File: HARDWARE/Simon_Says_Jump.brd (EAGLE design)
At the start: 57.1 x 88.9 mm, 35 parts, among them J1 RJ45, J2 RJ45, J3 RJ45, J4 RJ45, J6 5V, Q1 NPN, Q2 P-Channel MOSFET, Q3 NPN, Q4 P-Channel MOSFET, Q5 NPN, Q6 P-Channel MOSFET, Q7 NPN, Q8 P-Channel MOSFET, U1 3.3V Pro Mini, U2 RFM69_BOB

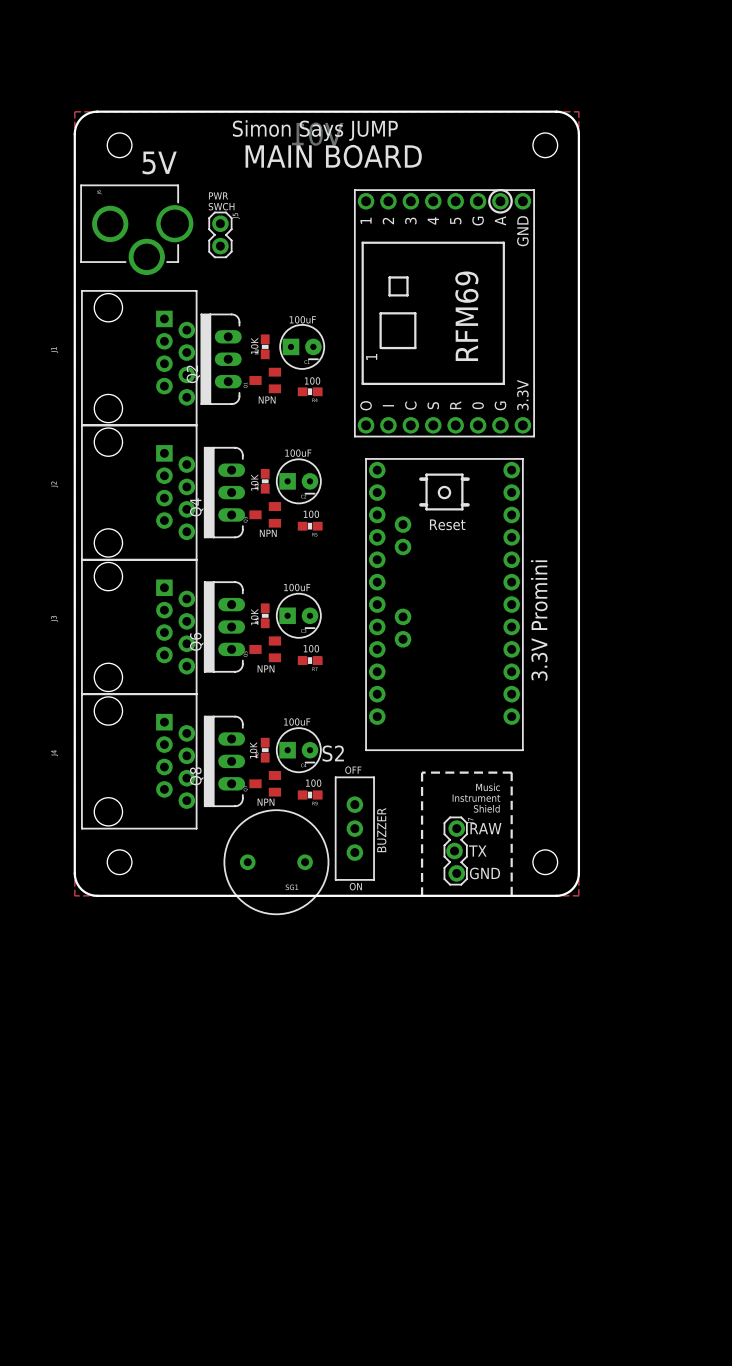
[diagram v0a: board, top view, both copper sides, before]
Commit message: logic level converters for the range finders
They need 5V Logic on trigger and echo pins.

Also, they're gonna need power (durp), so I stole one of the GND lines in the ethernet connectors/cables to be a dedicated 5V (aka RAW) to power the range sensors.
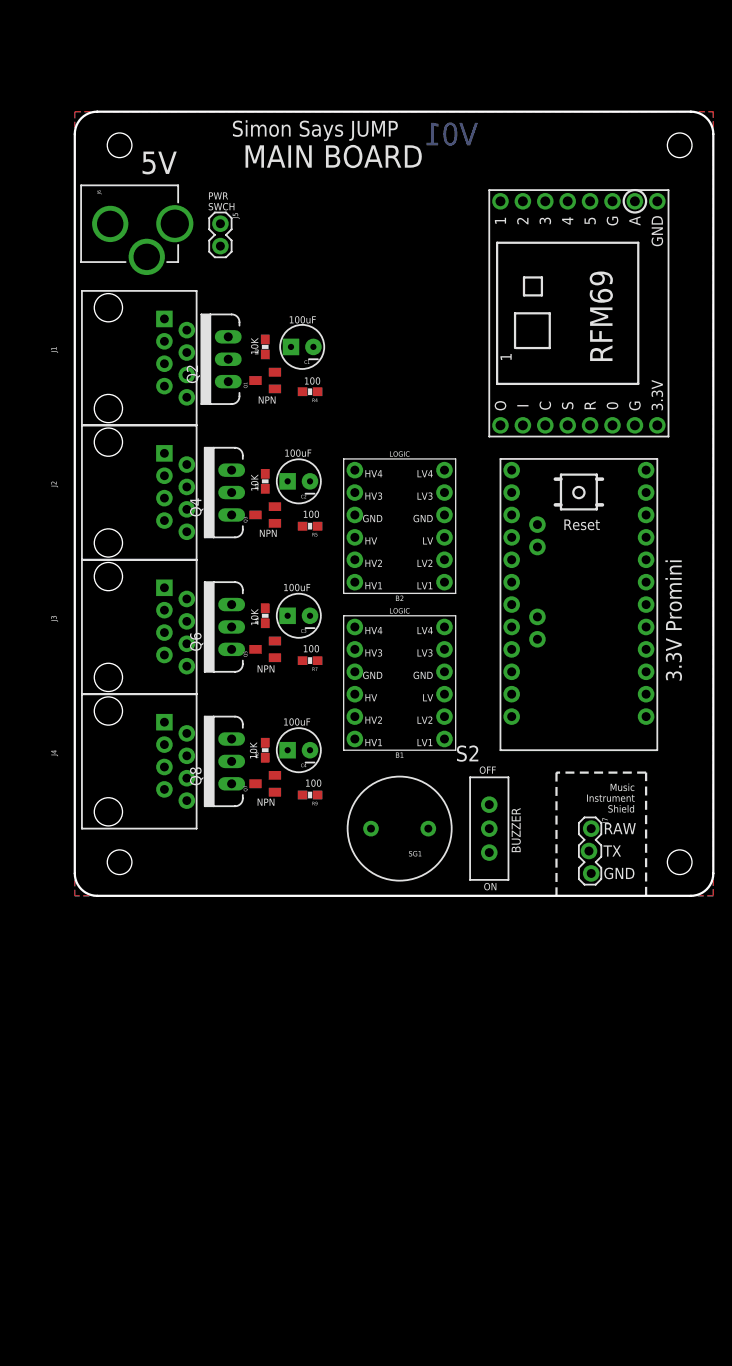
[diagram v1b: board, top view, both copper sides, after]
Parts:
- added B1, B2: LOGIC, SparkFun-Boards:SPARKFUN_LOGIC_LEVEL_CONVERTER
- moved U1 15.2 mm to (66.0, 49.5)
- moved J7 15.2 mm to (58.4, 7.62)
- moved S2 15.2 mm to (47.0, 7.62)
- moved U2 15.2 mm to (57.1, 66.0)
- moved JP2 15.2 mm to (68.6, 85.1)
- moved JP3 15.2 mm to (68.6, 3.81)
- moved SG1 14.5 mm to (36.8, 7.62)
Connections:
- new net ECHO1_5V: B2.HV1, J1.8
- new net ECHO2_5V: B2.HV2, J2.8
- new net ECHO3_5V: B2.HV3, J3.8
- new net ECHO4_5V: B2.HV4, J4.8
- new net RANGE_TRIGGER_5V: B1.HV1, J1.7, J2.7, J3.7, J4.7
- net 3.3V: now also B1.LV, B2.LV
- net ECHO1: now also B2.LV1; no longer J1.8
- net ECHO2: now also B2.LV2; no longer J2.8
- net ECHO3: now also B2.LV3; no longer J3.8
- net ECHO4: now also B2.LV4; no longer J4.8
- net GND: now also B1.GND1, B1.GND2, B2.GND1, B2.GND2; no longer J1.1, J2.1, J3.1, J4.1
- net RANGE_TRIGGER: now also B1.LV1, U1.D5; no longer J1.7, J2.7, J3.7, J4.7
- net RAW: now also B1.HV, B2.HV, J1.1, J2.1, J3.1, J4.1
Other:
- board size 57.1 x 88.9 mm -> 72.4 x 88.9 mm
- board text removed: "ROUTE OUT"

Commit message: About to switch to 3 trampoline control
Thought I'd do a commit here, because this could be a god fork point for the SFE installed 4-trampoline setup.
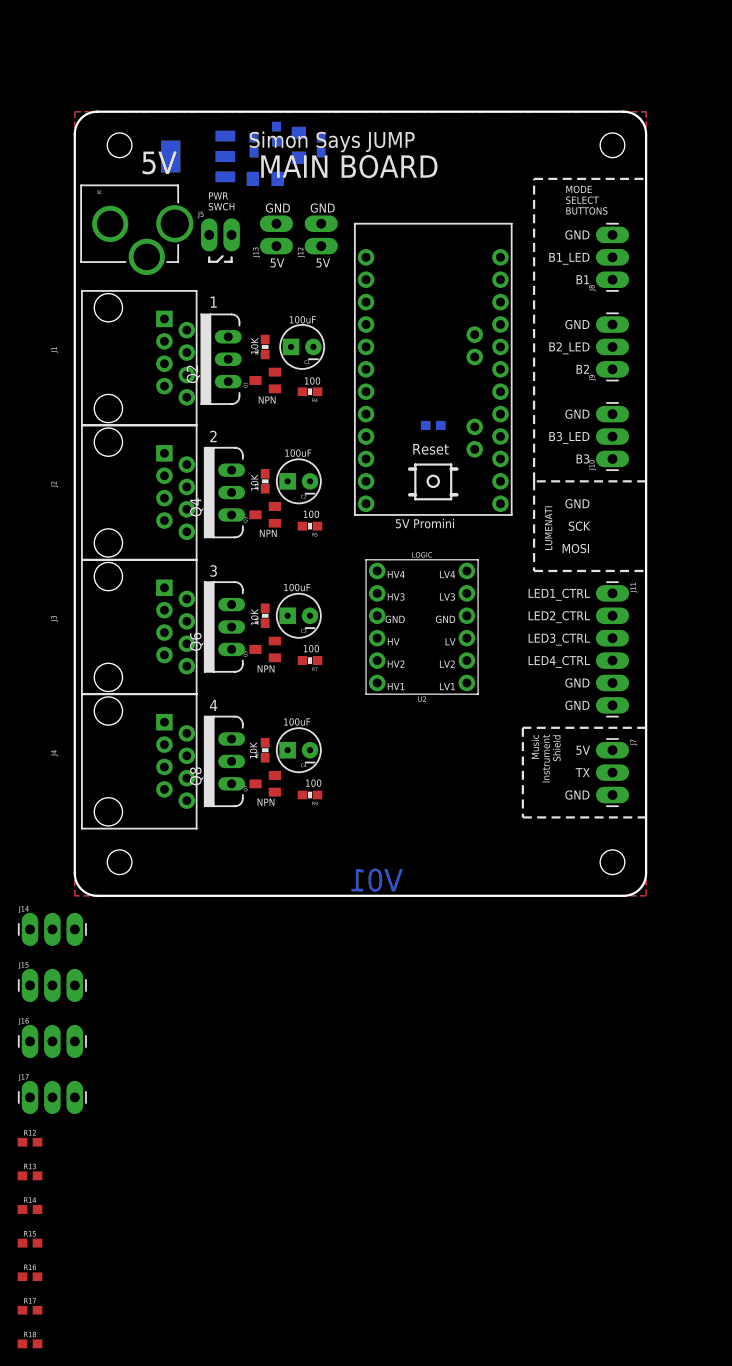
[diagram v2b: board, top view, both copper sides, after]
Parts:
- removed B1, B2: LOGIC, SparkFun-Boards:SPARKFUN_LOGIC_LEVEL_CONVERTER
- removed S2: (no value), SparkFun:SWITCH-SPDT_KIT
- removed SG1: BUZZER, SparkFun:BUZZER-12MM-KIT
- added C13: 0.1uF, SparkFun:0603-CAP
- added C5, C6: 10uF, SparkFun:EIA3216
- added IC1: (no value), SparkFun:SOT223
- added J10: B3, SparkFun-Connectors:1X03_LONGPADS
- added J11: (no value), SparkFun-Connectors:1X06_LONGPADS
- added J12, J13: (no value), SparkFun-Connectors:1X02_LONGPADS
- added J14: B4, SparkFun-Connectors:1X03_LONGPADS
- added J15: B5, SparkFun-Connectors:1X03_LONGPADS
- added J16: B6, SparkFun-Connectors:1X03_LONGPADS
- added J17: B7, SparkFun-Connectors:1X03_LONGPADS
- added J8: B1, SparkFun-Connectors:1X03_LONGPADS
- added J9: B2, SparkFun-Connectors:1X03_LONGPADS
- added R1: 390, SparkFun:0603-RES
- added R10: 240, SparkFun:0603-RES
- added R11: 10K, SparkFun:0603-RES
- added R12, R13, R14, R15, R16, R17, R18: 1k, SparkFun-Resistors:0603
- J5: device SparkFun-Connectors:1X02 -> SparkFun-Connectors:1X02_LONGPADS
- J7: device SparkFun-Connectors:1X03_LOCK -> SparkFun-Connectors:1X03_LONGPADS
- U1: value 3.3V Pro Mini -> 5V Pro Mini
- U2: value RFM69_BOB -> LOGIC; device SparkFun-Boards:RFM69_BOB -> SparkFun-Boards:SPARKFUN_LOGIC_LEVEL_CONVERTER
- moved U2 39.8 mm to (39.4, 30.5), turned to 180 degrees
- moved U1 34.9 mm to (31.8, 43.2), turned to 0 degrees
- moved J7 9.25 mm to (61.0, 16.5)
- moved JP2 7.62 mm to (61.0, 85.1)
- moved JP3 7.62 mm to (61.0, 3.81)
- moved J5 1.80 mm to (15.2, 74.9), turned to 0 degrees
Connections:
- removed net BUZZER1: SG1.+, U1.D4
- removed net BUZZER2: S2.3, U1.D7
- removed net D10: U1.D10, U2.S
- removed net D2: U1.D2, U2.0
- removed net ECHO1_5V: B2.HV1, J1.8
- removed net ECHO2_5V: B2.HV2, J2.8
- removed net ECHO3_5V: B2.HV3, J3.8
- removed net ECHO4_5V: B2.HV4, J4.8
- removed net MISO: U1.D12, U2.O
- removed net RANGE_TRIGGER_5V: B1.HV1, J1.7, J2.7, J3.7, J4.7
- removed net RAW: B1.HV, B2.HV, C1.1, C2.1, C3.1, C4.1, J1.1, J2.1, J3.1, J4.1, J5.2, J7.1, Q2.3, Q4.3, Q6.3, Q8.3, R2.2, R3.2, R6.2, R8.2, U1.RAW
- new net 5V: C1.1, C2.1, C3.1, C4.1, C6.A, IC1.3, J1.1, J12.1, J13.1, J2.1, J3.1, J4.1, J5.2, J7.1, Q2.3, Q4.3, Q6.3, Q8.3, R11.2, R2.2, R3.2, R6.2, R8.2, U1.VCC, U2.HV
- new net B1_LED: J8.2, U1.D8
- new net B2_LED: J9.2, U1.D9
- new net B3_LED: J10.2, U1.D10
- new net B4_LED: J14.2
- new net B5_LED: J15.2
- new net B6_LED: J16.2
- new net B7_LED: J17.2
- new net BUTTONS: R11.1, R12.1, U1.A7
- new net N$11: IC1.1, R1.2, R10.1
- new net N$13: J10.1, R14.2, R15.1
- new net N$14: J14.1, R15.2, R16.1
- new net N$15: J15.1, R16.2, R17.1
- new net N$16: J16.1, R17.2, R18.1
- new net N$17: J17.1, R18.2
- new net N$6: J9.1, R13.2, R14.1
- new net SW_SER_TX_3.3V: J7.2, U2.LV1
- net 3.3V: now also C13.1, C5.A, IC1.2, R10.2, U2.LV; no longer B1.LV, B2.LV, U1.VCC, U2.3.3V
- net ECHO1: now also J1.8, U1.D2; no longer B2.LV1, U1.D3
- net ECHO2: now also J2.8, U1.D3; no longer B2.LV2, U1.D6
- net ECHO3: now also J3.8, U1.D4; no longer B2.LV3, U1.D9
- net ECHO4: now also J4.8, U1.D5; no longer B2.LV4, U1.D8
- net GND: now also C13.2, C5.C, C6.C, J10.3, J11.5, J11.6, J12.2, J13.2, J14.3, J15.3, J16.3, J17.3, J8.3, J9.3, R1.1, U2.GND1, U2.GND2; no longer B1.GND1, B1.GND2, B2.GND1, B2.GND2, U2.G, U2.G2, U2.GND
- net LED1_CTRL: now also J11.1
- net LED2_CTRL: now also J11.2
- net LED3_CTRL: now also J11.3
- net LED4_CTRL: now also J11.4
- net MOSI: no longer U2.I
- net N$2: now also J8.1, R12.2, R13.1; no longer S2.2, SG1.-
- net RANGE_TRIGGER: now also J1.7, J2.7, J3.7, J4.7, U1.D6; no longer B1.LV1, U1.D5
- net SCK: no longer U2.C
- net SW_SER_TX: now also U2.HV1; no longer J7.2
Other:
- board size 72.4 x 88.9 mm -> 64.8 x 88.9 mm
- board text added: "1"
- board text added: "2"
- board text added: "3"
- board text added: "4"
- board text added: "5V Promini"
- board text added: "B1"
- board text added: "B1_LED"
- board text added: "B2"
- board text added: "B2_LED"
- board text added: "B3"
- board text added: "B3_LED"
- board text added: "LED1_CTRL"
- board text added: "LED2_CTRL"
- board text added: "LED3_CTRL"
- board text added: "LED4_CTRL"
- board text added: "LUMENATI"
- board text added: "MODE SELECT BUTTONS"
- board text added: "MOSI"
- board text added: "SCK"
- board text removed: "3.3V Promini"
- board text removed: "BUZZER"
- board text removed: "OFF"
- board text removed: "ON"
- board text removed: "RAW"

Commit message: Ready for layout
Opted to keep 4 trampoline/led controls. I ended up using some of the LED control lines as also control lines to the 7-segment, because I won't need to use both of these at the same time.

The toddler trampline is the only one that uses the 7-segment, and it will only use 2 buttons, so button 5,6,7 can be used for 7-segment.

Also added in 12V barrel jack input for 7-segment.

-added ethernet connector for control cable to overhead lights. These IO will control the beefcake relay boards that live up in the rafters with the can lights.
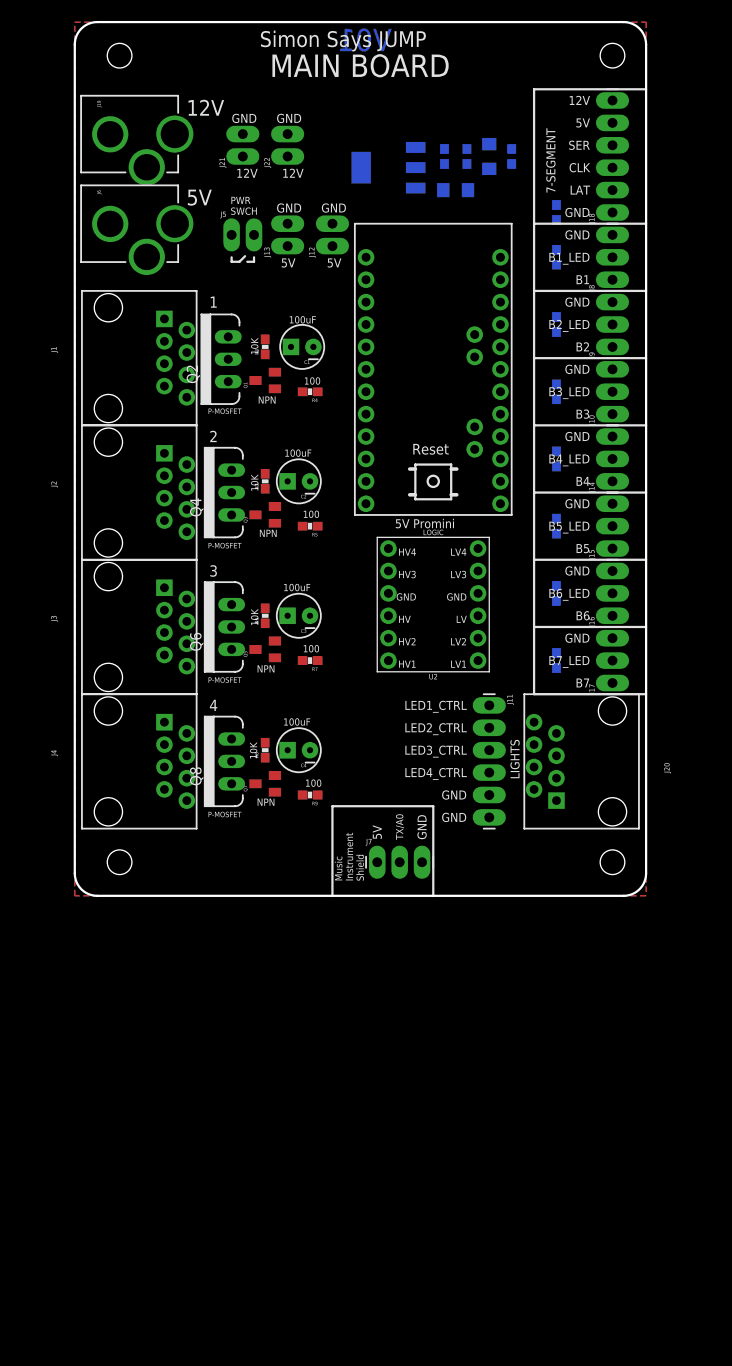
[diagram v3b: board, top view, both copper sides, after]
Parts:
- added J18: (no value), SparkFun-Connectors:1X06_LONGPADS
- added J19: 12V, SparkFun:POWER_JACK_PTH_LOCK
- added J20: RJ45, SparkFun-Connectors:RJ45-8
- added J21, J22: 12V, SparkFun-Connectors:1X02_LONGPADS
- J11: value (none) -> LED_CTRLS
- J12, J13: value (none) -> 5V
- moved R12 116.7 mm to (54.6, 72.4), flipped to the bottom, turned to 270 degrees
- moved R13 113.5 mm to (54.6, 64.8), flipped to the bottom, turned to 270 degrees
- moved R14 110.3 mm to (54.6, 57.1), flipped to the bottom, turned to 270 degrees
- moved R15 107.1 mm to (54.6, 49.5), flipped to the bottom, turned to 270 degrees
- moved R16 103.9 mm to (54.6, 41.9), flipped to the bottom, turned to 270 degrees
- moved R17 100.8 mm to (54.6, 34.3), flipped to the bottom, turned to 270 degrees
- moved R18 97.8 mm to (54.6, 26.7), flipped to the bottom, turned to 270 degrees
- moved J14 83.3 mm to (61.0, 47.0), turned to 90 degrees
- moved J15 82.6 mm to (61.0, 39.4), turned to 90 degrees
- moved J16 81.8 mm to (61.0, 31.8), turned to 90 degrees
- moved J17 81.1 mm to (61.0, 24.1), turned to 90 degrees
- moved J7 29.5 mm to (34.3, 3.81), turned to 0 degrees
- moved R11 27.9 mm to (54.6, 77.5), turned to 90 degrees
- moved R1 21.7 mm to (44.5, 83.8)
- moved C5 21.6 mm to (47.0, 83.8)
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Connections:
- removed net B5_LED: J15.2
- removed net B6_LED: J16.2
- removed net B7_LED: J17.2
- removed net MOSI: U1.D11
- removed net SCK: U1.D13
- new net 12V: J18.6, J19.PWR, J21.1, J22.1
- new net CLK/B6_LED: J16.2, J18.3, U1.D6
- new net LAT/B5_LED: J15.2, J18.2, U1.D5
- new net SER/B7_LED: J17.2, J18.4, U1.D7
- net 5V: now also J18.5
- net B1_LED: now also U1.D13; no longer U1.D8
- net B4_LED: now also U1.D11
- net ECHO4: now also U1.D8; no longer U1.D5
- net GND: now also J18.1, J19.GND, J19.GNDBREAK, J20.3, J20.6, J20.7, J20.8, J21.2, J22.2
- net LED1_CTRL: now also J20.1
- net LED2_CTRL: now also J20.2
- net LED3_CTRL: now also J20.4
- net LED4_CTRL: now also J20.5
- net RANGE_TRIGGER: now also U1.D12; no longer U1.D6
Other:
- board size 64.8 x 88.9 mm -> 64.8 x 99.1 mm
- board text added: ".01uF"
- board text added: "10uF"
- board text added: "12V"
- board text added: "240"
- board text added: "390"
- board text added: "7-SEGMENT"
- board text added: "ALL 1Ks"
- board text added: "B4"
- board text added: "B4_LED"
- board text added: "B5"
- board text added: "B5_LED"
- board text added: "B6"
- board text added: "B6_LED"
- board text added: "B7"
- board text added: "B7_LED"
- board text added: "CLK"
- board text added: "LAT"
- board text added: "LD1117"
- board text added: "LIGHTS"
- board text added: "SER"
- board text added: "TX/A0"
- board text removed: "100uf"
- board text removed: "LUMENATI"
- board text removed: "MODE SELECT BUTTONS"
- board text removed: "MOSI"
- board text removed: "SCK"
- board text removed: "TX"

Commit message: routing in progress 30 airwires left
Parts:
- moved J12 1.27 mm to (27.9, 73.7)
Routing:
- net 5V: track 0.00 -> 230.1 mm
- net RANGE_TRIGGER: track 0.00 -> 98.3 mm
- net ECHO4: track 0.00 -> 60.1 mm, vias 0 -> 2
- net 12V: track 0.00 -> 53.3 mm
- net ECHO3: track 0.00 -> 50.4 mm, vias 0 -> 1
- net ECHO2: track 0.00 -> 38.5 mm, vias 0 -> 1
- net ECHO1: track 0.00 -> 28.3 mm, vias 0 -> 1
- net N$6: track 0.00 -> 12.3 mm
- net N$2: track 0.00 -> 12.3 mm
- net N$15: track 0.00 -> 12.3 mm
- net N$14: track 0.00 -> 12.3 mm
- net N$16: track 0.00 -> 12.3 mm
- net N$13: track 0.00 -> 12.3 mm
- net 3.3V: track 0.00 -> 12.1 mm
- net LED4_PWR: track 0.00 -> 10.7 mm
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
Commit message: more layout coming along
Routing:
- net CLK/B6_LED: track 0.00 -> 129.5 mm, vias 0 -> 3
- net SER/B7_LED: track 0.00 -> 119.5 mm, vias 0 -> 1
- net LED2_CTRL: track 0.00 -> 110.2 mm, vias 0 -> 2
- net LAT/B5_LED: track 0.00 -> 88.8 mm
- net LED1_CTRL: track 0.00 -> 47.3 mm
- net LED4_CTRL: track 0.00 -> 43.4 mm
- net B2_LED: track 0.00 -> 41.6 mm, vias 0 -> 1
- net LED3_CTRL: track 0.00 -> 29.5 mm
- net B1_LED: track 0.00 -> 29.3 mm
- net BUTTONS: track 3.38 -> 31.4 mm, vias 0 -> 1
- net B3_LED: track 0.00 -> 24.7 mm, vias 0 -> 1
- net 5V: track 230.1 -> 244.7 mm
- net B4_LED: track 0.00 -> 13.8 mm
- net N$17: track 0.00 -> 7.05 mm
